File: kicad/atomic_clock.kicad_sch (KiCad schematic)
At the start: 34 parts, among them J1 Conn_02x05_Top_Bottom, J10 Conn_02x05_Top_Bottom, J11 Conn_02x05_Top_Bottom, J2 Conn_02x05_Top_Bottom, J3 Conn_02x05_Top_Bottom, J4 Conn_02x05_Top_Bottom, J5 USB_B_Micro, J6 Conn_02x05_Top_Bottom, J7 Conn_02x05_Top_Bottom, J8 Conn_02x05_Top_Bottom, J9 Conn_02x05_Top_Bottom, U1 D198K, U10 ATSAMDA1E16B-A, U11 D198K, U12 D198K, U13 D198K, U14 D198K, U15 D198K, U16 MAX7221xWG, U17 D198K, U18 D198K, U19 D198K, U2 D198K, U3 D198K, U4 D198K, U5 MAX7221xWG, U6 D198K, U7 D198K, U8 D198K, U9 D198K

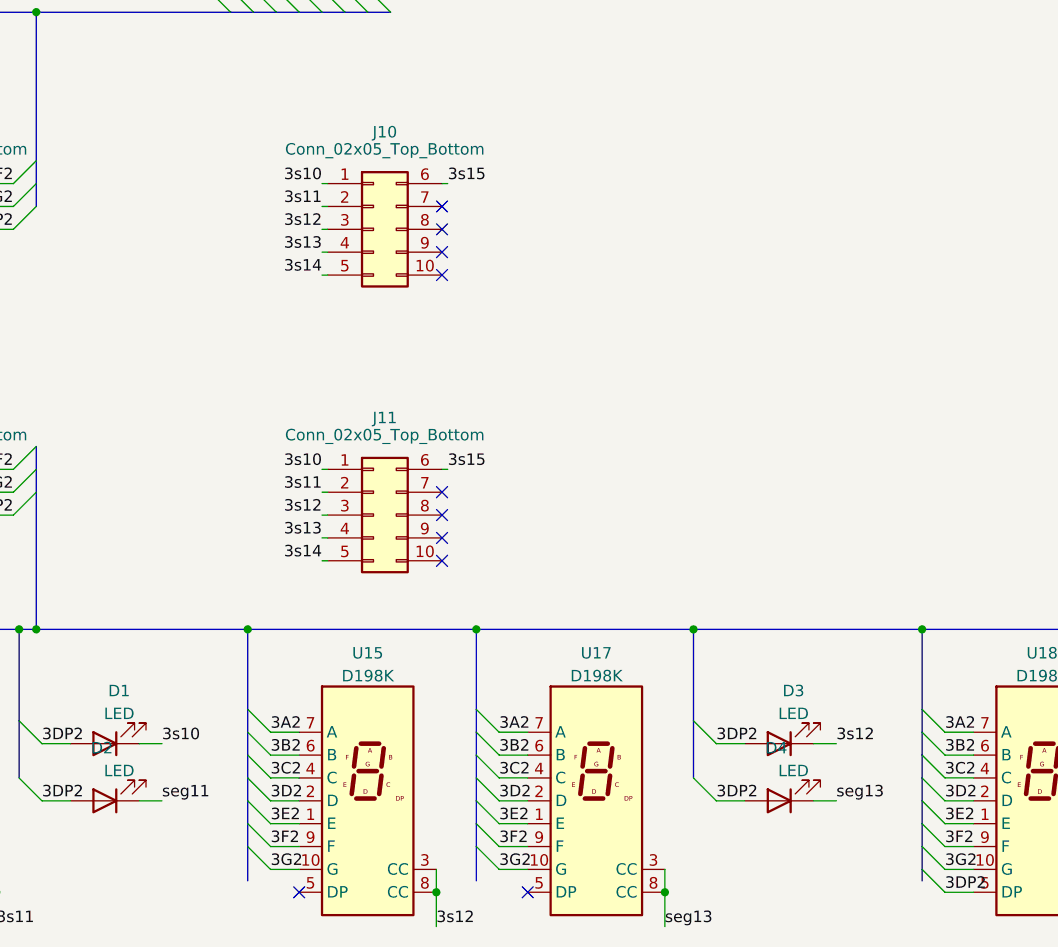
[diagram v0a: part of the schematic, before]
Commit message: Lay out part of PCB
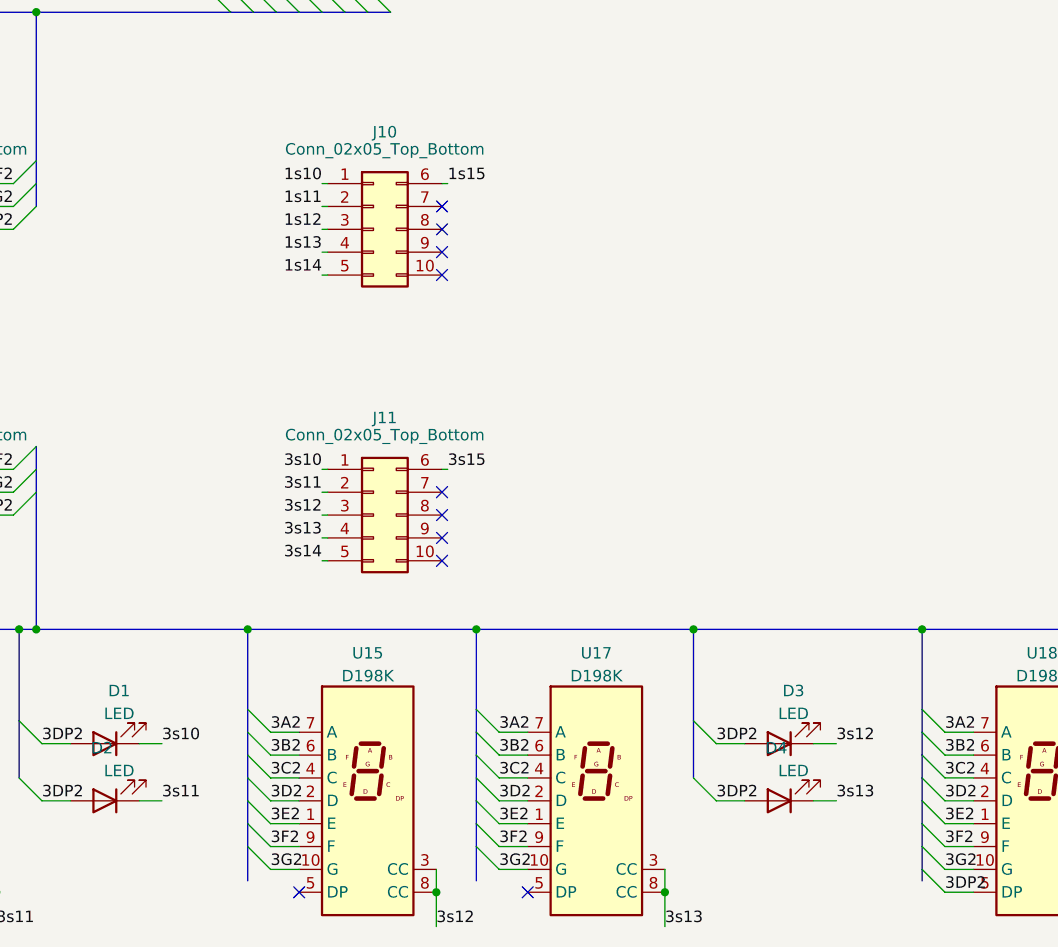
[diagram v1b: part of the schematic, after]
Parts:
- D1, D2, D3, D4: footprint (none) -> LED_THT:LED_D3.0mm_FlatTop
- U1, U2: footprint (none) -> Display_7Segment:D1X8K
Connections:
- net seg11 is gone; now on net 3s11: D2.1 (K)
- net seg13 is gone; now on net 3s13: D4.1 (K), U17.3 (CC), U17.8 (CC)
- net 1s10: now also J10.1 (Pin_1)
- net 1s11: now also J10.2 (Pin_2)
- net 1s12: now also J10.3 (Pin_3)
- net 1s13: now also J10.4 (Pin_4)
- net 1s14: now also J10.5 (Pin_5)
- net 1s15: now also J10.6 (Pin_6)
- net 3s10: no longer J10.1 (Pin_1)
- net 3s11: no longer J10.2 (Pin_2)
- net 3s12: no longer J10.3 (Pin_3)
- net 3s13: no longer J10.4 (Pin_4)
- net 3s14: no longer J10.5 (Pin_5)
- net 3s15: no longer J10.6 (Pin_6)
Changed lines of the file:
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@@
     (effects (font (size 1.27 1.27)) (justify left bottom))
   )
-  (label "seg13" (at 450.85 318.77 0)
+  (label "3s13" (at 450.85 318.77 0)
     (effects (font (size 1.27 1.27)) (justify left bottom))
   )
@@
     (effects (font (size 1.27 1.27)) (justify left bottom))
   )
-  (label "3s11" (at 412.75 238.76 180)
+  (label "1s11" (at 412.75 238.76 180)
     (effects (font (size 1.27 1.27)) (justify right bottom))
   )
@@
     (effects (font (size 1.27 1.27)) (justify left bottom))
   )
-  (label "3s13" (at 412.75 243.84 180)
+  (label "1s13" (at 412.75 243.84 180)
     (effects (font (size 1.27 1.27)) (justify right bottom))
   )
@@
     (effects (font (size 1.27 1.27)) (justify right bottom))
   )
-  (label "seg11" (at 394.97 304.8 0)
+  (label "3s11" (at 394.97 304.8 0)
     (effects (font (size 1.27 1.27)) (justify left bottom))
   )
@@
     (effects (font (size 1.27 1.27)) (justify left bottom))
   )
-  (label "seg13" (at 469.9 304.8 0)
+  (label "3s13" (at 469.9 304.8 0)
     (effects (font (size 1.27 1.27)) (justify left bottom))
   )
@@
     (effects (font (size 1.27 1.27)) (justify left bottom))
   )
-  (label "3s10" (at 412.75 236.22 180)
+  (label "1s10" (at 412.75 236.22 180)
     (effects (font (size 1.27 1.27)) (justify right bottom))
   )
@@
     (effects (font (size 1.27 1.27)) (justify left bottom))
   )
-  (label "3s14" (at 412.75 246.38 180)
+  (label "1s14" (at 412.75 246.38 180)
     (effects (font (size 1.27 1.27)) (justify right bottom))
   )
@@
     (effects (font (size 1.27 1.27)) (justify left bottom))
   )
-  (label "3s15" (at 426.72 236.22 0)
+  (label "1s15" (at 426.72 236.22 0)
     (effects (font (size 1.27 1.27)) (justify left bottom))
   )
@@
     (effects (font (size 1.27 1.27)) (justify left bottom))
   )
-  (label "3s12" (at 412.75 241.3 180)
+  (label "1s12" (at 412.75 241.3 180)
     (effects (font (size 1.27 1.27)) (justify right bottom))
   )
@@
     (property "Reference" "D3" (id 0) (at 465.1375 292.5912 0))
     (property "Value" "LED" (id 1) (at 465.1375 295.1281 0))
-    (property "Footprint" "" (id 2) (at 463.55 298.45 0)
+    (property "Footprint" "LED_THT:LED_D3.0mm_FlatTop" (id 2) (at 463.55 298.45 0)
       (effects (font (size 1.27 1.27)) hide)
     )
@@
     (property "Reference" "D1" (id 0) (at 390.2075 292.5912 0))
     (property "Value" "LED" (id 1) (at 390.2075 295.1281 0))
-    (property "Footprint" "" (id 2) (at 388.62 298.45 0)
+    (property "Footprint" "LED_THT:LED_D3.0mm_FlatTop" (id 2) (at 388.62 298.45 0)
       (effects (font (size 1.27 1.27)) hide)
     )
@@
     (property "Reference" "U2" (id 0) (at 113.03 288.4002 0))
     (property "Value" "D198K" (id 1) (at 113.03 290.9371 0))
-    (property "Footprint" "" (id 2) (at 113.03 320.04 0)
+    (property "Footprint" "Display_7Segment:D1X8K" (id 2) (at 113.03 320.04 0)
       (effects (font (size 1.27 1.27)) hide)
     )
@@
     (property "Reference" "U1" (id 0) (at 87.63 288.4002 0))
     (property "Value" "D198K" (id 1) (at 87.63 290.9371 0))
-    (property "Footprint" "" (id 2) (at 87.63 320.04 0)
+    (property "Footprint" "Display_7Segment:D1X8K" (id 2) (at 87.63 320.04 0)
       (effects (font (size 1.27 1.27)) hide)
     )
@@
     (property "Reference" "D4" (id 0) (at 463.2325 298.9412 0))
     (property "Value" "LED" (id 1) (at 465.1375 301.4781 0))
-    (property "Footprint" "" (id 2) (at 463.55 304.8 0)
+    (property "Footprint" "LED_THT:LED_D3.0mm_FlatTop" (id 2) (at 463.55 304.8 0)
       (effects (font (size 1.27 1.27)) hide)
     )
@@
     (property "Reference" "D2" (id 0) (at 388.3025 298.9412 0))
     (property "Value" "LED" (id 1) (at 390.2075 301.4781 0))
-    (property "Footprint" "" (id 2) (at 388.62 304.8 0)
-      (effects (font (size 1.27 1.27)) hide)
-    )
+    (property "Footprint" "LED_THT:LED_D3.0mm_FlatTop" (id 2) (at 388.62 304.8 0)
+      (effects (font (size 1.27 1.27)) hide)
+    )

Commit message: Progress on PCB
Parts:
- added C1, C6, C7: 100nF, Capacitor_SMD:C_0805_2012Metric, symbol Device:C
- added C2, C3: 10uF, Capacitor_SMD:C_0805_2012Metric, symbol Device:C
- added C4, C5: C, Capacitor_SMD:C_0805_2012Metric, symbol Device:C
- added J12: USB_B_Micro, Connector_USB:USB_Micro-B_Amphenol_10118194_Horizontal, symbol Connector:USB_B_Micro
- added J13: Conn_ARM_JTAG_SWD_10, local_footprints:sam_swd_header, symbol Connector:Conn_ARM_JTAG_SWD_10
- added J14: (no value), symbol Connector:Conn_01x03_Female
- added R1, R3, R4: 10K, Resistor_SMD:R_0805_2012Metric, symbol Device:R
- added R2: 1K, Resistor_SMD:R_0805_2012Metric, symbol Device:R
- added U20: NCP1117LPST33T3G, Package_TO_SOT_SMD:SOT-223, symbol local_symbols:NCP1117LPST33T3G
- added U21: mems_osc_st1630, Package_TO_SOT_SMD:SOT-23-5, symbol local_symbols:mems_osc_st1630
- added U?: (no value), symbol local_symbols:DHT20
- J5: footprint Connector_USB:USB_Micro-B_Amphenol_10118194_Horizontal -> (none)
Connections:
- net 5V: now also C1.1, C2.1, C7.1, J12.1 (VBUS), R1.2, R4.2, U20.3 (VIN); no longer U10.29 (VDDCORE), U10.30 (VDDIN), U10.9 (VDDANA)
- net GND: now also J5.6 (Shield), C1.2, C2.2, C3.2, C4.2, C5.2, C6.2, C7.2, J12.5 (GND), J12.6 (Shield), J13.3 (GND), J13.5 (GND), J14.1 (Pin_1), R2.2, U20.1 (GND), U20.4 (SINK), U21.1 (GND), U21.2 (NC/GND), U21.3 (NC/GND), U?.3 (GND)
- net UART_RX: now also J14.2 (Pin_2)
- net UART_TX: now also J14.3 (Pin_3)
- net at U5.1 (DIN): now also U10.11 (PA08)
- net at U5.12 (~{CS}): now also U10.13 (PA10)
- net at U5.13 (CLK): now also U10.12 (PA09), U16.13 (CLK)
- net at U5.18 (ISET): now also R1.1
- net at U5.24 (DOUT): now also U16.1 (DIN)
- net at U16.12 (~{CS}): now also U10.14 (PA11)
- net at U16.18 (ISET): now also R4.1
- net XIN32: now reaches U10.1 (PA00)
- net XIN32: now also U21.5 (CLK_Out)
- net at U10.26 (~{RESET}): now also C6.1, J13.10 (~{RESET}), R3.1
- net SWCLK: now reaches U10.31 (PA30)
- net SWCLK: now also J13.4 (SWDCLK/TCK), R2.1
- net SWDIO: now reaches U10.32 (PA31)
- net SWDIO: now also J13.2 (SWDIO/TMS)
- new net: C5.1, U10.29 (VDDCORE)
- new net 3.3V: C3.1, C4.1, J13.1 (VTref), R3.2, U10.30 (VDDIN), U10.9 (VDDANA), U20.2 (VOUT), U21.4 (VDD), U?.1 (VDD)
- no-connect marks 57 -> 47
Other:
- note added: "Horizontal USB connector Power only"
- note added: "Vertical USB connector Power and data"
- moved on the sheet: U10

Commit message: Layout mostly done.
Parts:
- added C8: 100nF, Capacitor_SMD:C_0805_2012Metric, symbol Device:C
- added D5: (no value), symbol Device:D
- added D6: D, symbol Device:D
- added R5: (no value), symbol Device:R
- added R6: R_Photo, OptoDevice:R_LDR_4.9x4.2mm_P2.54mm_Vertical, symbol Device:R_Photo
- added U23: (no value), symbol local_symbols:DCF77
- J14: value (none) -> Conn_01x03_Female; footprint (none) -> Connector_PinSocket_2.54mm:PinSocket_1x03_P2.54mm_Vertical
- J5: footprint (none) -> Connector_USB:USB_Micro-B_Molex-105133-0001
- U22: renamed from U?; value (none) -> DHT20
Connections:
- net 3.3V: now also C8.1, R5.1, U23.1 (VCC)
- net 5V: now also D5.1 (K), D6.1 (K); no longer J12.1 (VBUS), J5.1 (VBUS)
- net GND: now also C8.2, U23.2 (GND)
- net UART_RX: now also U10.7 (PA06_/SER0_PAD2); no longer U10.5 (PA04)
- net UART_TX: now also U10.5 (PA04_/SER0_PAD0); no longer U10.4 (PA03)
- net USB+: now also U10.24 (PA25_SER3_PAD3/SER5_PAD3); no longer U10.25 (PA27)
- net USB-: now also U10.23 (PA24_SER3_PAD2/SER5_PAD2); no longer U10.24 (PA25)
- net DO: now reaches U10.11 (PA08_SER0_PAD0/SER2_PAD0), U5.1 (DIN)
- net ~SS: now reaches U10.13 (PA10_SER0_PAD2/SER2_PAD2), U5.12 (~{CS})
- net ~SS: now also U16.12 (~{CS})
- net SCK: now reaches U10.12 (PA09_SER0_PAD1/SER2_PAD1), U16.13 (CLK), U5.13 (CLK)
- net at U10.14 (PA11_SER0_PAD3/SER2_PAD3): no longer U16.12 (~{CS})
- net at U10.17 (PA16_SER1_PAD0/SER3_PAD0): now also U22.2 (SDA)
- net at U10.18 (PA17_SER1_PAD1/SER3_PAD1): now also U22.4 (SCL)
- net DCF_DATA: now reaches U10.21 (PA22_SER3_PAD0/SER5_PAD0)
- net DCF_DATA: now also U23.4 (DO)
- net DCF_PDN: now reaches U10.22 (PA23_SER3_PAD1/SER5_PAD1)
- net DCF_PDN: now also U23.5 (DI/PDN)
- net LDR: now reaches U10.3 (PA02)
- net LDR: now also R5.2, R6.2
- new net: D6.2 (A), J5.1 (VBUS)
- new net: D5.2 (A), J12.1 (VBUS)
- new net LDR_SINK: R6.1, U10.25 (PA27)
- no-connect marks 47 -> 42
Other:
- moved on the sheet: J14, U10, U21, U22

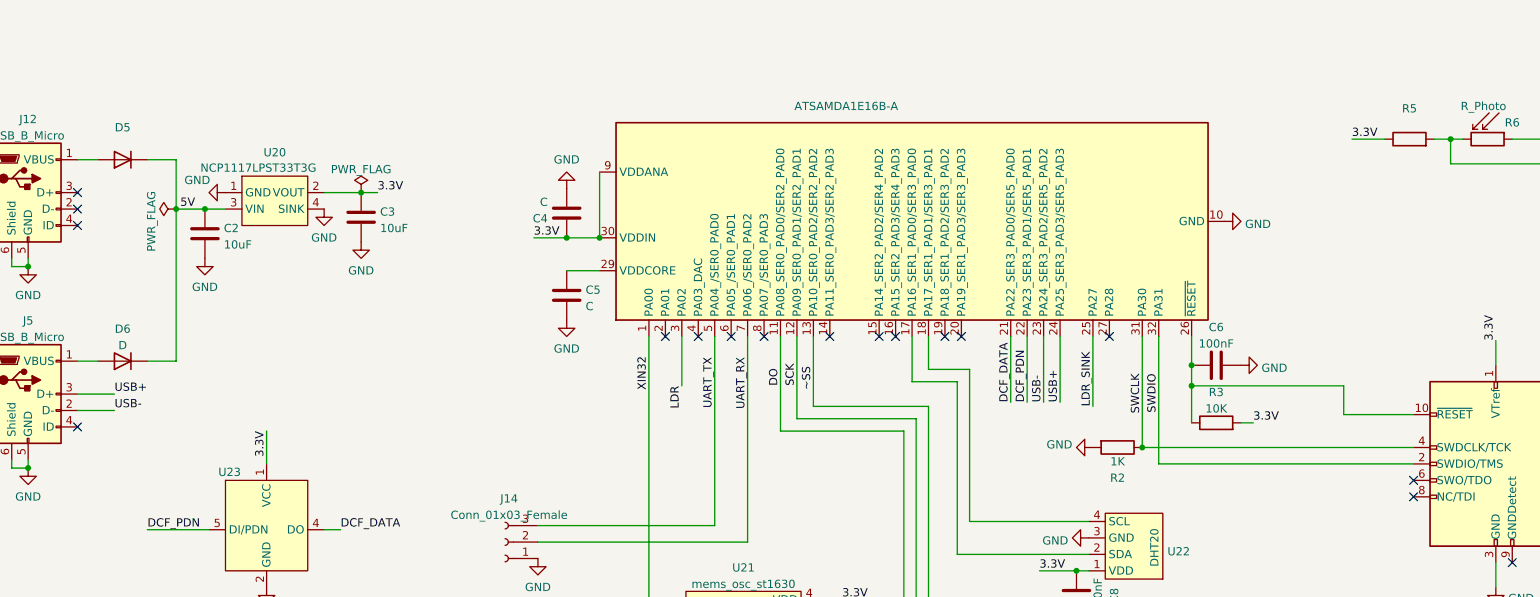
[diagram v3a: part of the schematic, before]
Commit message: Stretch PCB to accommodate the LDR.
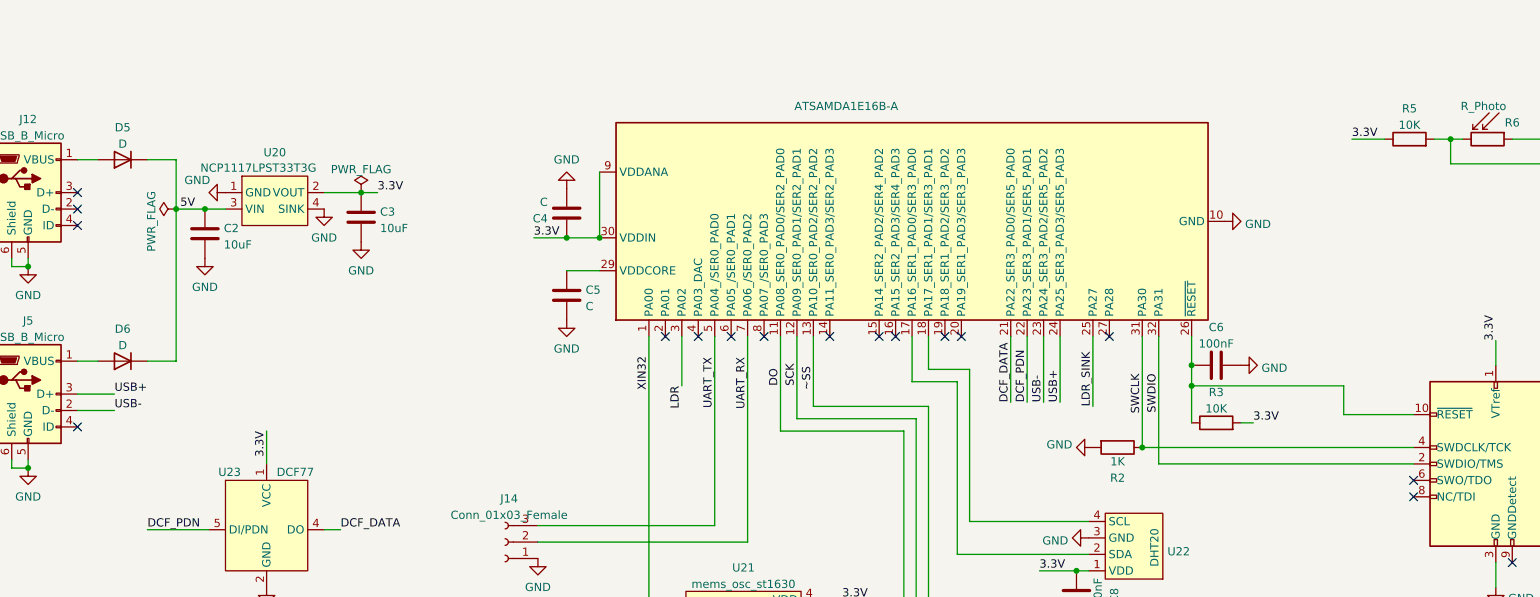
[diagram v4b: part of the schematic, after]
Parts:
- D5: value (none) -> D
- R5: value (none) -> 10K; footprint (none) -> Resistor_SMD:R_0805_2012Metric
- U22: footprint (none) -> local_footprints:DHT20
- U23: value (none) -> DCF77; footprint (none) -> local_footprints:DCF77 receiver module
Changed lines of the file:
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@@
     (in_bom yes) (on_board yes)
     (property "Reference" "U23" (id 0) (at 208.915 142.24 0))
-    (property "Value" "" (id 1) (at 219.075 142.24 0))
-    (property "Footprint" "" (id 2) (at 214.63 149.86 0)
+    (property "Value" "DCF77" (id 1) (at 219.075 142.24 0))
+    (property "Footprint" "local_footprints:DCF77 receiver module" (id 2) (at 214.63 149.86 0)
       (effects (font (size 1.27 1.27)) hide)
     )
@@
     (in_bom yes) (on_board yes) (fields_autoplaced)
     (property "Reference" "D5" (id 0) (at 192.405 89.0102 0))
-    (property "Value" "" (id 1) (at 192.405 91.5471 0))
+    (property "Value" "D" (id 1) (at 192.405 91.5471 0))
     (property "Footprint" "" (id 2) (at 192.405 93.98 0)
       (effects (font (size 1.27 1.27)) hide)
@@
     (in_bom yes) (on_board yes) (fields_autoplaced)
     (property "Reference" "R5" (id 0) (at 391.16 86.0892 90))
-    (property "Value" "" (id 1) (at 391.16 88.6261 90))
-    (property "Footprint" "" (id 2) (at 391.16 92.583 90)
+    (property "Value" "10K" (id 1) (at 391.16 88.6261 90))
+    (property "Footprint" "Resistor_SMD:R_0805_2012Metric" (id 2) (at 391.16 92.583 90)
       (effects (font (size 1.27 1.27)) hide)
     )
@@
       (effects (font (size 1.27 1.27)) (justify left))
     )
-    (property "Footprint" "" (id 2) (at 344.17 152.4 0)
+    (property "Footprint" "local_footprints:DHT20" (id 2) (at 344.17 152.4 0)
       (effects (font (size 1.27 1.27)) hide)
     )
@@
     )
     (path "/9ad349d5-a248-4ca5-aef5-ebd538d72f9a"
-      (reference "D5") (unit 1) (value "D") (footprint "")
+      (reference "D5") (unit 1) (value "D") (footprint "Diode_SMD:D_SMA")
     )
     (path "/294e3ea7-d3eb-4300-8d36-8b57e51708b7"
-      (reference "D6") (unit 1) (value "D") (footprint "")
+      (reference "D6") (unit 1) (value "D") (footprint "Diode_SMD:D_SMA")
     )
     (path "/520717c6-bdac-4bb0-8fa6-caa1dba8a4af"

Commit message: Reworked battery/power system
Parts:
- added BT1: (no value), symbol Device:Battery_Cell
- added C10, C9: (no value), Capacitor_SMD:C_0805_2012Metric, symbol Device:C
- added D7: (no value), symbol Device:LED
- added D8, D9: (no value), symbol Device:D
- added Q1: (no value), symbol Device:Q_Dual_PMOS_S1G1D2S2G2D1
- added R10, R11, R12, R13, R14, R15: 10K, Capacitor_SMD:C_0805_2012Metric, symbol Device:R
- added R7, R8: (no value), Capacitor_SMD:C_0805_2012Metric, symbol Device:R
- added R9: 10K, Resistor_SMD:R_0805_2012Metric, symbol Device:R
- added SW1: (no value), symbol Switch:SW_Push
- added U24: MCP73831-2-OT, Package_TO_SOT_SMD:SOT-23-5, symbol Battery_Management:MCP73831-2-OT
- D5, D6: value D -> (none)
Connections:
- net 3.3V: now also Q1.1 (S), R9.2; no longer C8.1, U22.1 (VDD), U23.1 (VCC)
- net 5V: now also C9.1, D8.2 (A), R10.1, R8.2, U24.4 (VDD); no longer C2.1, U20.3 (VIN)
- net DCF_DATA: now also U10.7 (PA06_/SER0_PAD2); no longer U10.21 (PA22_SER3_PAD0/SER5_PAD0)
- net DCF_PDN: now also U10.8 (PA07_/SER0_PAD3); no longer U10.22 (PA23_SER3_PAD1/SER5_PAD1)
- net GND: now also BT1.2 (-), C10.1, C9.2, R12.2, R15.1, SW1.2, U24.2 (VSS)
- net UART_RX: now also U10.22 (PA23_SER3_PAD1/SER5_PAD1); no longer U10.7 (PA06_/SER0_PAD2)
- net UART_TX: now also U10.21 (PA22_SER3_PAD0/SER5_PAD0); no longer U10.5 (PA04_/SER0_PAD0)
- net SWITCH: now reaches U10.16 (PA15_SER2_PAD3/SER4_PAD3)
- net SWITCH: now also R9.1, SW1.1
- net pwr_sense: now reaches U10.6 (PA05_/SER0_PAD1)
- net pwr_sense: now also R10.2, R11.1
- net ~SS renamed ~{SS}
- new net: R11.2, R12.1
- new net: BT1.1 (+), C10.2, D9.2 (A), U24.3 (VBAT)
- new net: R7.1, U24.5 (PROG)
- new net: R14.1, R7.2
- new net: D7.1 (K), U24.1 (STAT)
- new net: C2.1, D8.1 (K), D9.1 (K), U20.3 (VIN)
- new net: R13.2, R14.2
- new net: D7.2 (A), R8.1
- new net: R13.1, R15.2
- new net 3.3V_peripherals: C8.1, Q1.6 (D), U22.1 (VDD), U23.1 (VCC)
- new net ~{peripheral_ctrl}: Q1.2 (G), U10.5 (PA04_/SER0_PAD0)
- no-connect marks 42 -> 39
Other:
- note added: "3.6V rechargeable LiPo battery only!"
- note added: "40k for 25mA charging current."
- moved on the sheet: C2, C3, D5, D6, J12, J14, J5, U20, U23

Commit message: Finished PCB placement
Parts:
- added unit 2 of Q1
- added Q2: (no value), symbol Device:Q_Dual_PMOS_S1G1D2S2G2D1
- added U25: (no value), Package_TO_SOT_SMD:SOT-363_SC-70-6, symbol local_symbols:TXB0101
- BT1: value (none) -> Battery_Cell; footprint (none) -> local_footprints:Battery_pads
- C10, C9: value (none) -> 4.7uF
- D5, D6, D8, D9: value (none) -> D; footprint (none) -> Diode_SMD:D_SMA
- D7: value (none) -> LED; footprint (none) -> LED_SMD:LED_1206_3216Metric_Pad1.42x1.75mm_HandSolder
- Q1: value (none) -> Q_Dual_PMOS; footprint (none) -> Package_TO_SOT_SMD:SOT-363_SC-70-6
- R10, R11, R12, R13, R14, R15: footprint Capacitor_SMD:C_0805_2012Metric -> (none)
- R7: value (none) -> 10K; footprint Capacitor_SMD:C_0805_2012Metric -> (none)
- R8: value (none) -> 330R; footprint Capacitor_SMD:C_0805_2012Metric -> (none)
- SW1: value (none) -> SW_Push; footprint (none) -> Button_Switch_SMD:SW_SPST_TL3342
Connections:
- net 3.3V: now also Q1.4 (S), U25.1 (VCCA), U25.5 (OE)
- net 5V: now also Q2.6 (D); no longer D5.1 (K), D6.1 (K), D8.2 (A), R10.1
- net GND: now also U25.2 (GND)
- net ~{DCF_CTL}: now reaches U10.4 (PA03_DAC)
- net ~{DCF_CTL}: now also Q1.5 (G)
- net 3.3V_peripherals renamed PERIPHERAL_PWR
- net PERIPHERAL_PWR: no longer U23.1 (VCC)
- net ~{peripheral_ctrl} renamed ~{PERIPHERAL_CTL}
- net ~{PERIPHERAL_CTL}: now also U25.3 (A)
- new net: D5.1 (K), D6.1 (K), D8.2 (A), Q2.1 (S), R10.1, U25.6 (VCCB)
- new net: Q2.2 (G), U25.4 (B)
- new net 3.3V_DCF: Q1.3 (D), U23.1 (VCC)
- no-connect marks 39 -> 38
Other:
- title: (none) -> DCF-77 Radio controlled clock
- moved on the sheet: D5, D6, J12, R10, R11, R12
